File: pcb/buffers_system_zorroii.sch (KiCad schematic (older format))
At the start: 37 parts, among them U5 74LVCH162245A

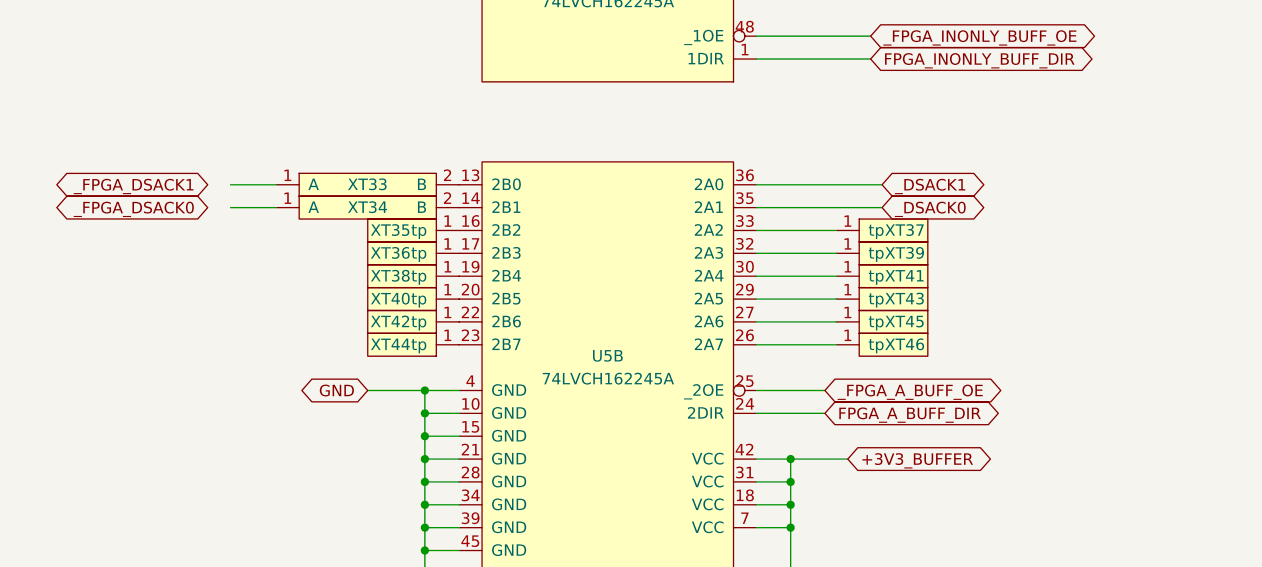
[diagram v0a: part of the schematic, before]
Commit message: Unused buffer io are now grounded via testpads
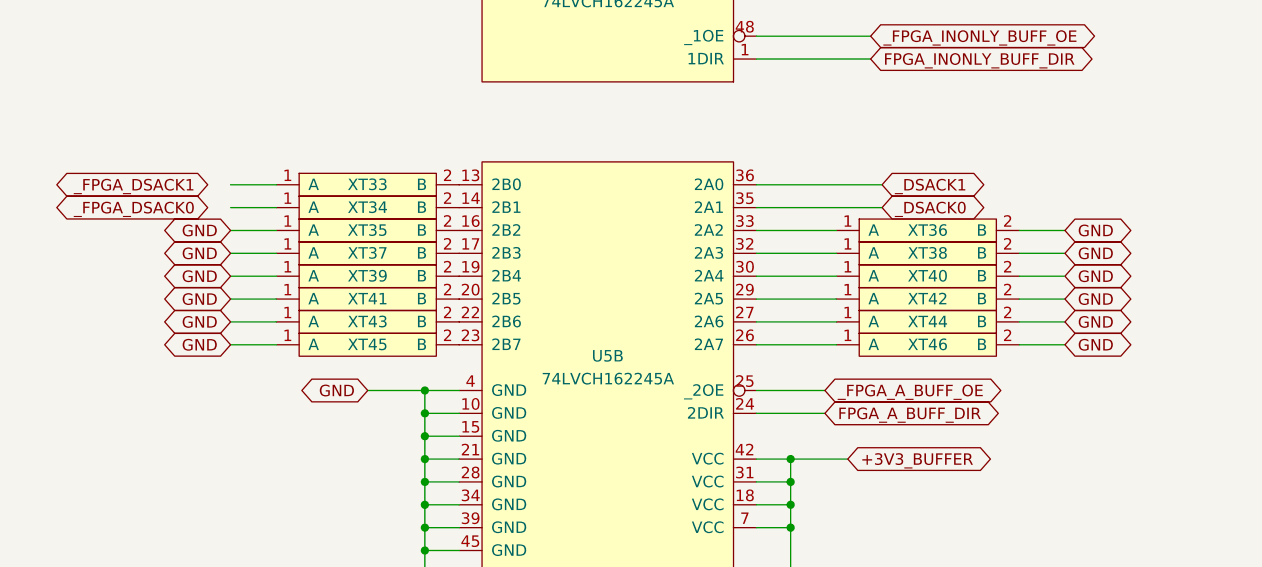
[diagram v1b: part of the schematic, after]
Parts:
- removed XT35, XT36, XT37, XT38, XT39, XT40, XT41, XT42, XT43, XT44, XT45, XT46: testpoint, WM1200:testpoint, symbol WM1200:testpoint
- added XT35, XT36, XT37, XT38, XT39, XT40, XT41, XT42, XT43, XT44, XT45, XT46: testpoint_cutline, WM1200:testpoint_cutline, symbol WM1200:testpoint_cutline
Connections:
- wire segments 90 -> 102

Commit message: Some work done, sync
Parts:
- C17, C18, C19, C20: footprint Capacitor_SMD:C_0603_1608Metric_Pad1.05x0.95mm_HandSolder -> Capacitor_SMD:C_0402_1005Metric
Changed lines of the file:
@@
 F 0 "C17" V 4402 5200 50  0000 C CNN
 F 1 "0.1uF 35V" V 4311 5200 50  0000 C CNN
-F 2 "Capacitor_SMD:C_0603_1608Metric_Pad1.05x0.95mm_HandSolder" H 4188 5050 50  0001 C CNN
+F 2 "Capacitor_SMD:C_0402_1005Metric" H 4188 5050 50  0001 C CNN
 F 3 "~" H 4150 5200 50  0001 C CNN
 	1    4150 5200
@@
 F 0 "C18" V 4402 5600 50  0000 C CNN
 F 1 "0.1uF 35V" V 4311 5600 50  0000 C CNN
-F 2 "Capacitor_SMD:C_0603_1608Metric_Pad1.05x0.95mm_HandSolder" H 4188 5450 50  0001 C CNN
+F 2 "Capacitor_SMD:C_0402_1005Metric" H 4188 5450 50  0001 C CNN
 F 3 "~" H 4150 5600 50  0001 C CNN
 	1    4150 5600
@@
 F 0 "C19" V 4402 6000 50  0000 C CNN
 F 1 "0.1uF 35V" V 4311 6000 50  0000 C CNN
-F 2 "Capacitor_SMD:C_0603_1608Metric_Pad1.05x0.95mm_HandSolder" H 4188 5850 50  0001 C CNN
+F 2 "Capacitor_SMD:C_0402_1005Metric" H 4188 5850 50  0001 C CNN
 F 3 "~" H 4150 6000 50  0001 C CNN
 	1    4150 6000
@@
 F 0 "C20" V 4402 6400 50  0000 C CNN
 F 1 "0.1uF 35V" V 4311 6400 50  0000 C CNN
-F 2 "Capacitor_SMD:C_0603_1608Metric_Pad1.05x0.95mm_HandSolder" H 4188 6250 50  0001 C CNN
+F 2 "Capacitor_SMD:C_0402_1005Metric" H 4188 6250 50  0001 C CNN
 F 3 "~" H 4150 6400 50  0001 C CNN
 	1    4150 6400

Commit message: some dirty routing
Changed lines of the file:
@@
 Text GLabel 5100 4200 2    50   BiDi ~ 0
 FPGA_A_BUFF_DIR
-Text GLabel 2400 3300 0    50   BiDi ~ 0
+Text GLabel 2500 3300 0    50   BiDi ~ 0
 _FPGA_DSACK0
-Text GLabel 2400 3200 0    50   BiDi ~ 0
+Text GLabel 2500 3200 0    50   BiDi ~ 0
 _FPGA_DSACK1
 Wire Wire Line
@@
 	5200 4400 4950 4400
 Connection ~ 4950 4400
-Text GLabel 6150 2050 2    50   BiDi ~ 0
+Text GLabel 6100 2050 2    50   BiDi ~ 0
 _FPGA_BERR
-Text GLabel 6150 2150 2    50   BiDi ~ 0
+Text GLabel 6100 2150 2    50   BiDi ~ 0
 FPGA_CPUCLK_A
-Text GLabel 6150 1950 2    50   BiDi ~ 0
+Text GLabel 6100 1950 2    50   BiDi ~ 0
 _FPGA_HLT
-Text GLabel 6150 1650 2    50   BiDi ~ 0
+Text GLabel 6100 1650 2    50   BiDi ~ 0
 _FPGA_IPL2
-Text GLabel 6150 1550 2    50   BiDi ~ 0
+Text GLabel 6100 1550 2    50   BiDi ~ 0
 _FPGA_IPL1
-Text GLabel 6150 1750 2    50   BiDi ~ 0
+Text GLabel 6100 1750 2    50   BiDi ~ 0
 _FPGA_IPL0
-Text GLabel 6150 1850 2    50   BiDi ~ 0
+Text GLabel 6100 1850 2    50   BiDi ~ 0
 _FPGA_RST
-Text GLabel 6150 2250 2    50   BiDi ~ 0
+Text GLabel 6100 2250 2    50   BiDi ~ 0
 _FPGA_KBRESET
 Text GLabel 5300 2550 2    50   BiDi ~ 0
